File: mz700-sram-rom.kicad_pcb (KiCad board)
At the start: 2 copper layers, 94 x 65.4 mm, 19 parts, among them J1 JTAG, J2 MZ700Bus-2014-single-row, SW1 SW_DIP_x05, U1 ATF1502-44, U2 74HCT688, U3 74HCT670, U4 74HCT670, U5 AS6C1008, U6 28C64

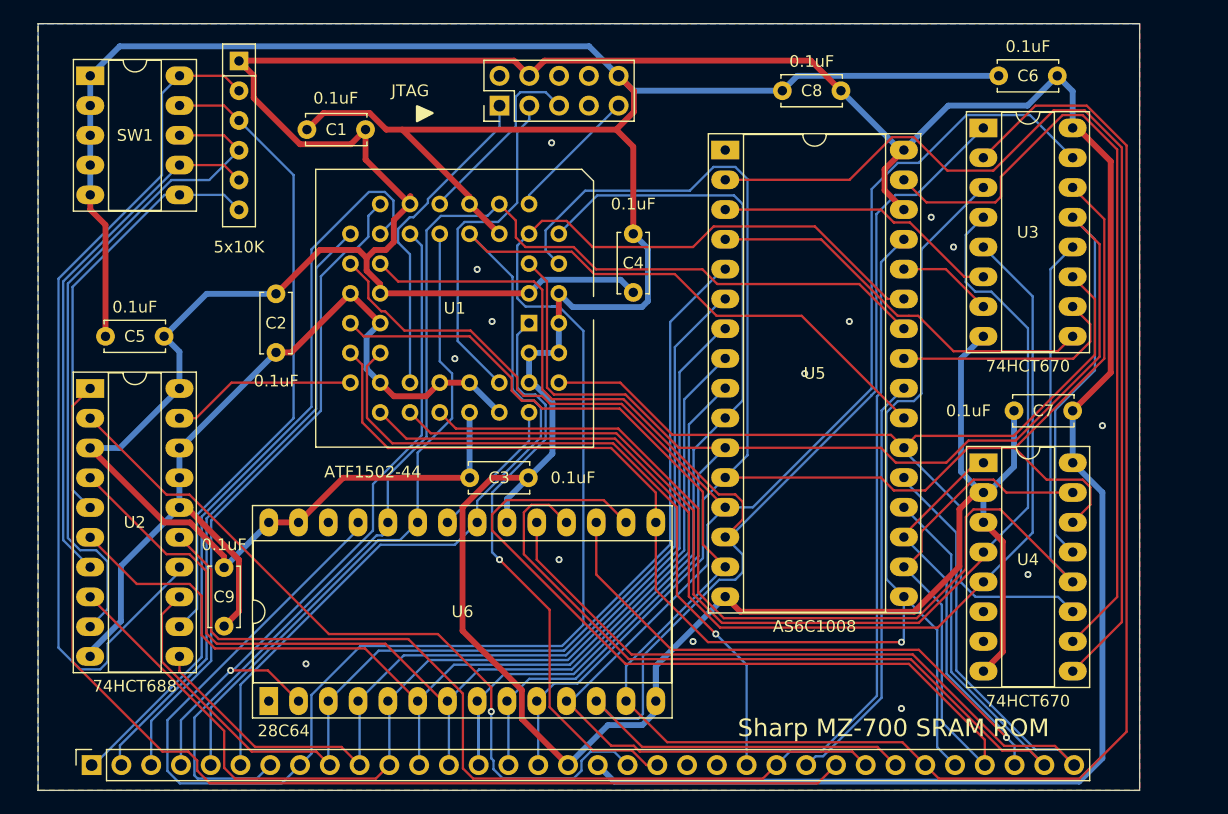
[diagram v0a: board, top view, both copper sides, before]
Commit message: 1.3
Added logic to disable the board is $D000->$FFFF is locked ($E5) or DRAM ($E1)
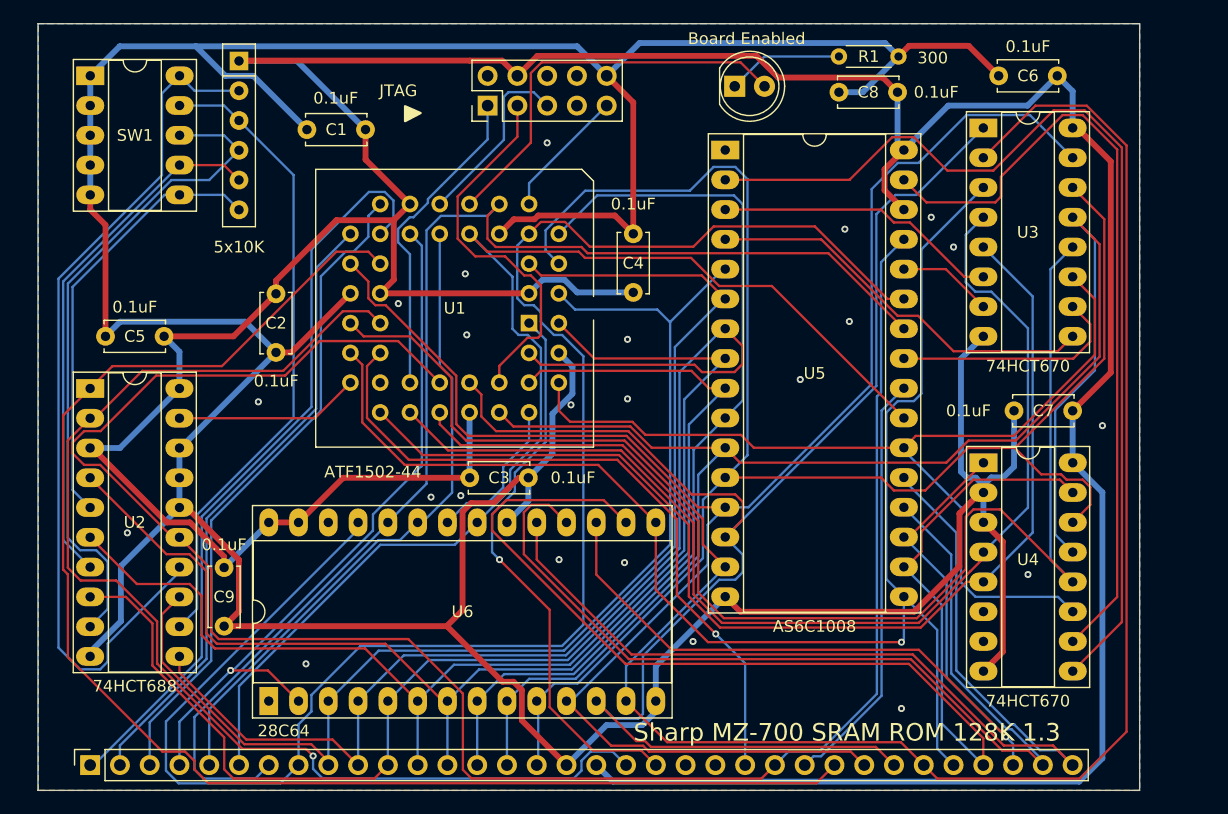
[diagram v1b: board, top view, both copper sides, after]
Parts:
- added D1: Board Enabled, LED_THT:LED_D5.0mm, F.Cu at (143.3, 80.3)
- added R1: 300, Resistor_THT:R_Axial_DIN0204_L3.6mm_D1.6mm_P5.08mm_Horizontal, F.Cu at (152.1, 77.7)
- moved C8 4.83 mm to (157.1, 80.8)
- moved J1 1.02 mm to (122.2, 81.9)
- moved J2 0.13 mm to (88.3, 138.2)
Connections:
- U1 pad 11: GND -> Net-(D1-A)
- U1 pad 2: GND -> /A7
- U1 pad 21: /D1 -> /~{IORQ}
- U1 pad 25: GND -> /~{M1}
- U1 pad 34: GND -> /~{WR}
- U1 pad 36: GND -> /D1
- U1 pad 37: GND -> /A1
- U1 pad 41: GND -> /A3
- U1 pad 43: GND -> /A5
- U1 pad 44: GND -> /A4
- U1 pad 5: /A1 -> /A6
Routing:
- net /~{WR}: track 117.7 -> 167.1 mm
- net /~{M1}: track 64.5 -> 102.2 mm
- net Net-(D1-A): track 0.00 -> 34.5 mm
- net /~{IORQ}: track 94.5 -> 125.0 mm
- net /A5: track 90.3 -> 114.8 mm
- net /A6: track 80.7 -> 98.6 mm
- net /A3: track 89.0 -> 105.8 mm
- net /D1: track 146.5 -> 129.8 mm
- net GND: track 399.1 -> 382.8 mm, vias 14 -> 23
- net /A4: track 87.1 -> 101.9 mm
- net /A7: track 89.7 -> 100.2 mm
- net Net-(D1-K): track 0.00 -> 9.94 mm
- net /A1: track 146.1 -> 138.1 mm
- net /A2: track 84.2 -> 78.1 mm
- net Net-(J1-Pin_3): track 29.3 -> 32.5 mm
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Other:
- board text added: "Sharp MZ-700 SRAM ROM 128K 1.3"
- board text removed: "Sharp MZ-700 SRAM ROM"

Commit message: added board id
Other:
- board text added: "ST-401"
- board text added: "Sharp MZ-700 128K SRAM 8K ROM 1.3"
- board text removed: "Sharp MZ-700 SRAM ROM 128K 1.3"
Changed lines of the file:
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@@
 		(tags "Resistor Axial_DIN0204 series Axial Horizontal pin pitch 5.08mm 0.167W length 3.6mm diameter 1.6mm")
 		(property "Reference" "R1"
-			(at 2.54 0 360)
+			(at 2.54 0 0)
 			(layer "F.SilkS")
 			(effects
@@
 		)
 		(fp_text user "${REFERENCE}"
-			(at 2.54 0 360)
+			(at 2.54 0 0)
 			(layer "F.Fab")
 			(effects
@@
 		(layer "Edge.Cuts")
 	)
-	(gr_text "Sharp MZ-700 SRAM ROM 128K 1.3"
-		(at 134.62 136.271 0)
+	(gr_text "ST-401"
+		(at 85.3948 135.6106 0)
 		(layer "F.SilkS")
 		(effects
 			(font
 				(size 1.5 1.5)
-				(thickness 0.1875)
+				(thickness 0.3)
+				(bold yes)
+			)
+			(justify left bottom)
+		)
+	)
+	(gr_text "Sharp MZ-700 128K SRAM 8K ROM 1.3"
+		(at 131.1656 136.4996 0)
+		(layer "F.SilkS")
+		(effects
+			(font
+				(size 1.5 1.5)
+				(thickness 0.3)
+				(bold yes)
 			)
 			(justify left bottom)

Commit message: cleanup
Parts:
- added Ref**: Val**, sharpox:logo.cdr, F.Cu at (141.8, 132.6)
- D1: footprint LED_THT:LED_D5.0mm -> LED_THT:LED_D3.0mm
- moved D1 0.34 mm to (143.3, 80.6)
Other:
- board size 94 x 65.4 mm -> 95.2 x 65.4 mm
- board text added: "Sharp MZ-700 128K SRAM+8K ROM 1.3"
- board text removed: "Sharp MZ-700 128K SRAM 8K ROM 1.3"

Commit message: update
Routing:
- net GND: track 382.8 -> 368.7 mm, vias 23 -> 29
- net /~{MMU_WR}: track 104.6 -> 101.0 mm
- net /~{IORQ}: track 125.0 -> 126.8 mm
- net /RA1: track 96.5 -> 97.6 mm
- net Net-(D1-A): track 34.7 -> 33.7 mm
- net +5V: track 330.7 -> 331.6 mm
- net /A4: track 101.9 -> 102.5 mm

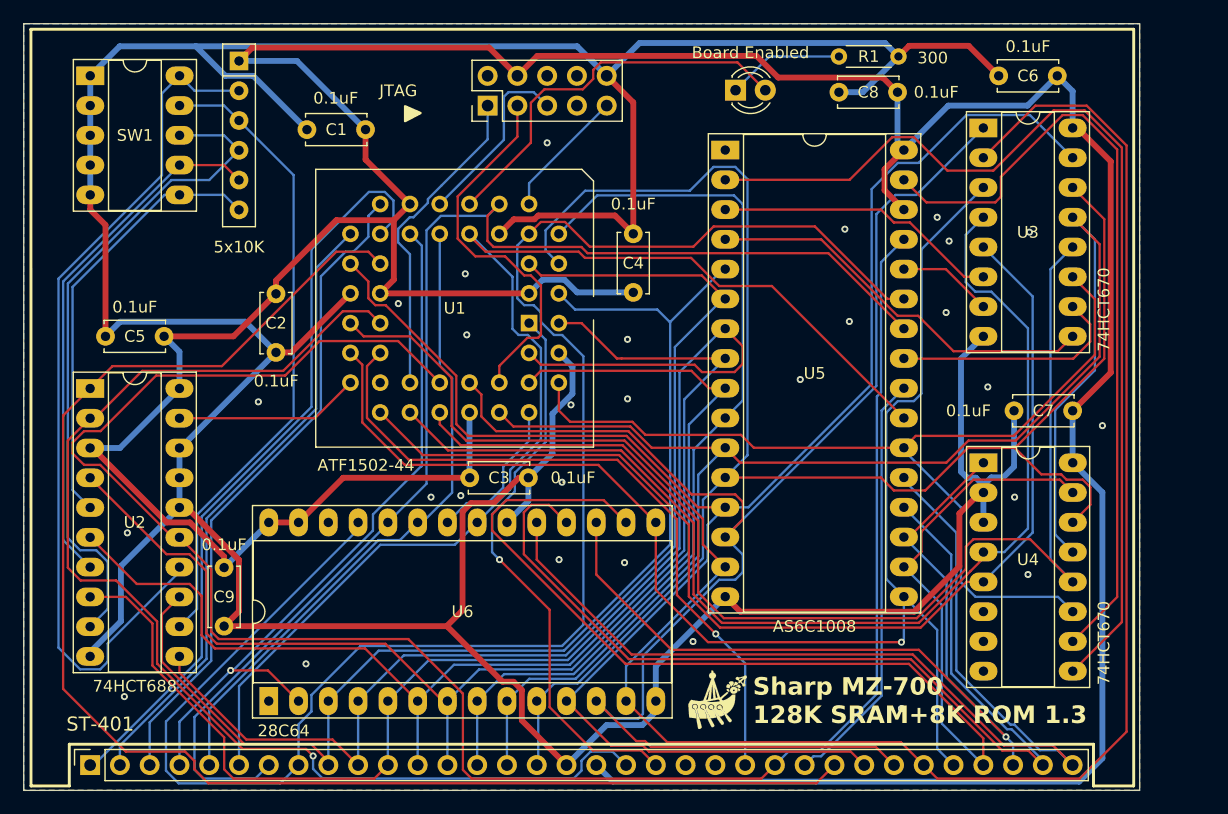
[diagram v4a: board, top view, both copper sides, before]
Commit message: replaced LED from cpld with transistor
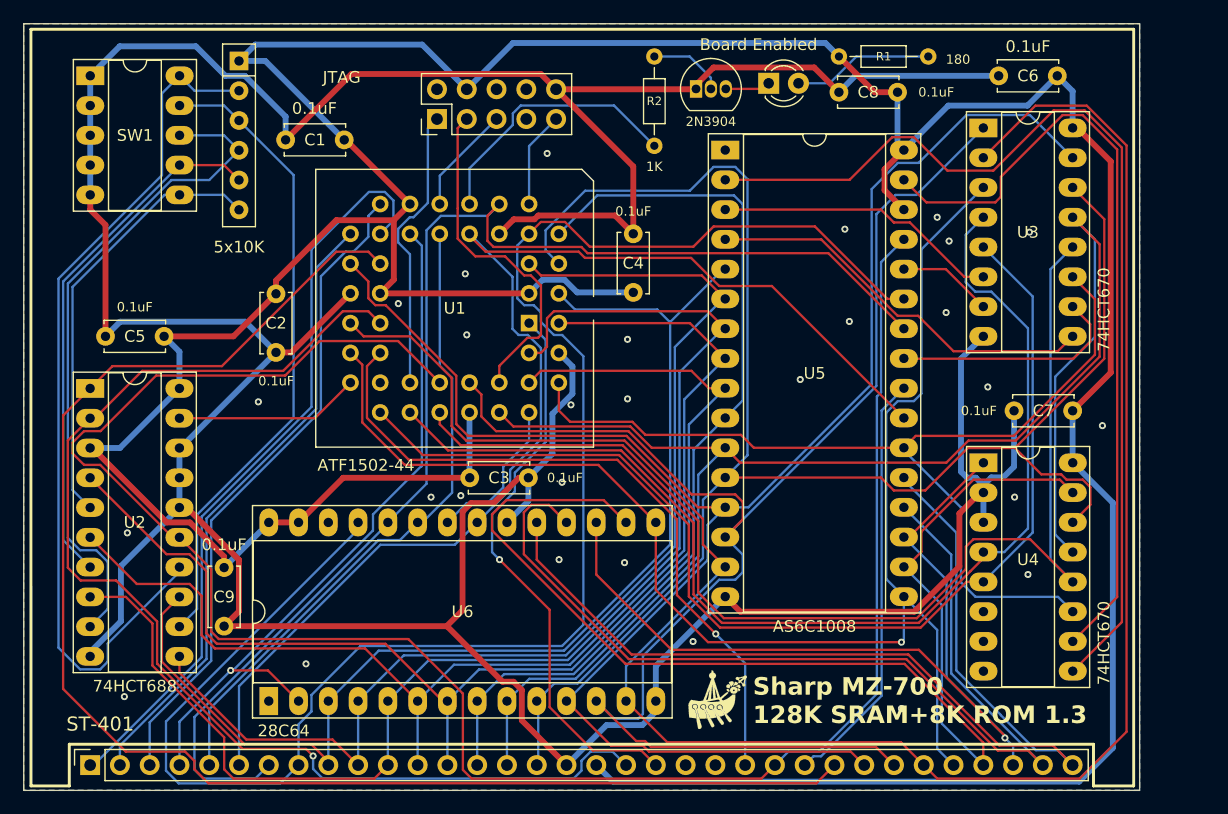
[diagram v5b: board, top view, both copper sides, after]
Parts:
- removed D1: Board Enabled, LED_THT:LED_D3.0mm
- added D2: Board Enabled, LED_THT:LED_D3.0mm, F.Cu at (146.2, 80.0)
- added Q1: 2N3904, Package_TO_SOT_THT:TO-92_Inline, F.Cu at (140.0, 80.5)
- added R2: 1K, Resistor_THT:R_Axial_DIN0204_L3.6mm_D1.6mm_P7.62mm_Horizontal, F.Cu at (136.4, 85.3)
- R1: value 300 -> 180; footprint Resistor_THT:R_Axial_DIN0204_L3.6mm_D1.6mm_P5.08mm_Horizontal -> Resistor_THT:R_Axial_DIN0204_L3.6mm_D1.6mm_P7.62mm_Horizontal
- moved J1 4.47 mm to (117.9, 83.1)
- moved C1 2.02 mm to (109.9, 84.8)
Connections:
- R1 pad 1: Net-(D1-K) -> +5V
- R1 pad 2: GND -> Net-(D2-A)
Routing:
- net GND: track 368.7 -> 356.2 mm
- net Net-(D2-A): track 0.00 -> 12.0 mm
- net Net-(U1-PD1/I/O): track 33.7 -> 23.0 mm
- net Net-(D1-K): track 10.0 -> 0.00 mm
- net Net-(Q1-B): track 0.00 -> 6.53 mm
- net Net-(J1-Pin_5): track 15.7 -> 9.26 mm
- net Net-(D2-K): track 0.00 -> 3.86 mm
- net Net-(J1-Pin_9): track 11.1 -> 8.21 mm
- net Net-(J1-Pin_1): track 27.4 -> 24.5 mm
- net Net-(J1-Pin_3): track 32.5 -> 29.6 mm
- net /A5: track 114.8 -> 112.2 mm
- net +5V: track 331.6 -> 332.9 mm
